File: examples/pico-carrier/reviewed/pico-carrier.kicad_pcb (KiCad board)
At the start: 2 copper layers, 82 x 68 mm, 9 parts, among them J1 5V IN, J3 GP0-GP15, J4 GP16-GP28, PWR, U1 Pico

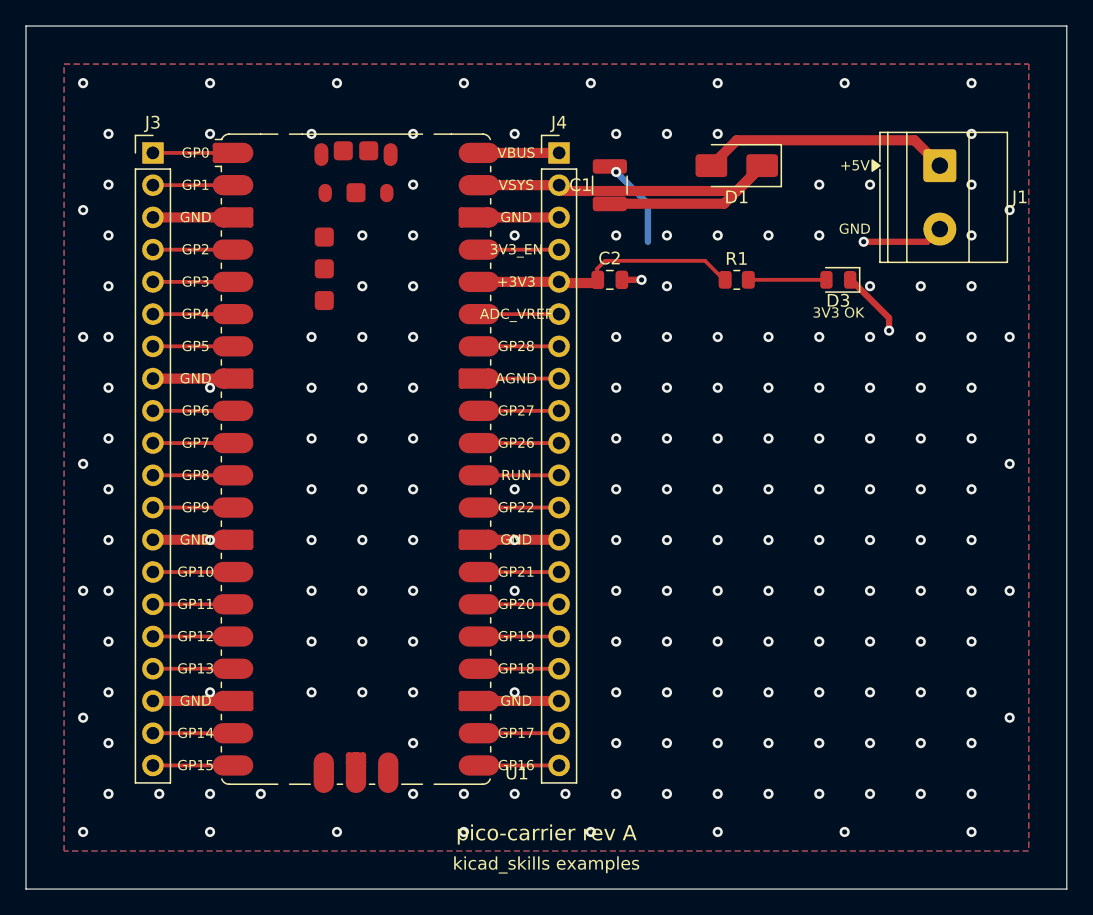
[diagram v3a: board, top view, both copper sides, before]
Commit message: Regenerate the four boards whose corners were off the grid
Ninety-one bends at angles nobody chose, now none. All four still pass
their gates.

Co-Authored-By: Claude Fable 5 <noreply@anthropic.com>
Claude-Session: https://claude.ai/code/session_01DUj7Ltu92tWg159mCSacwY
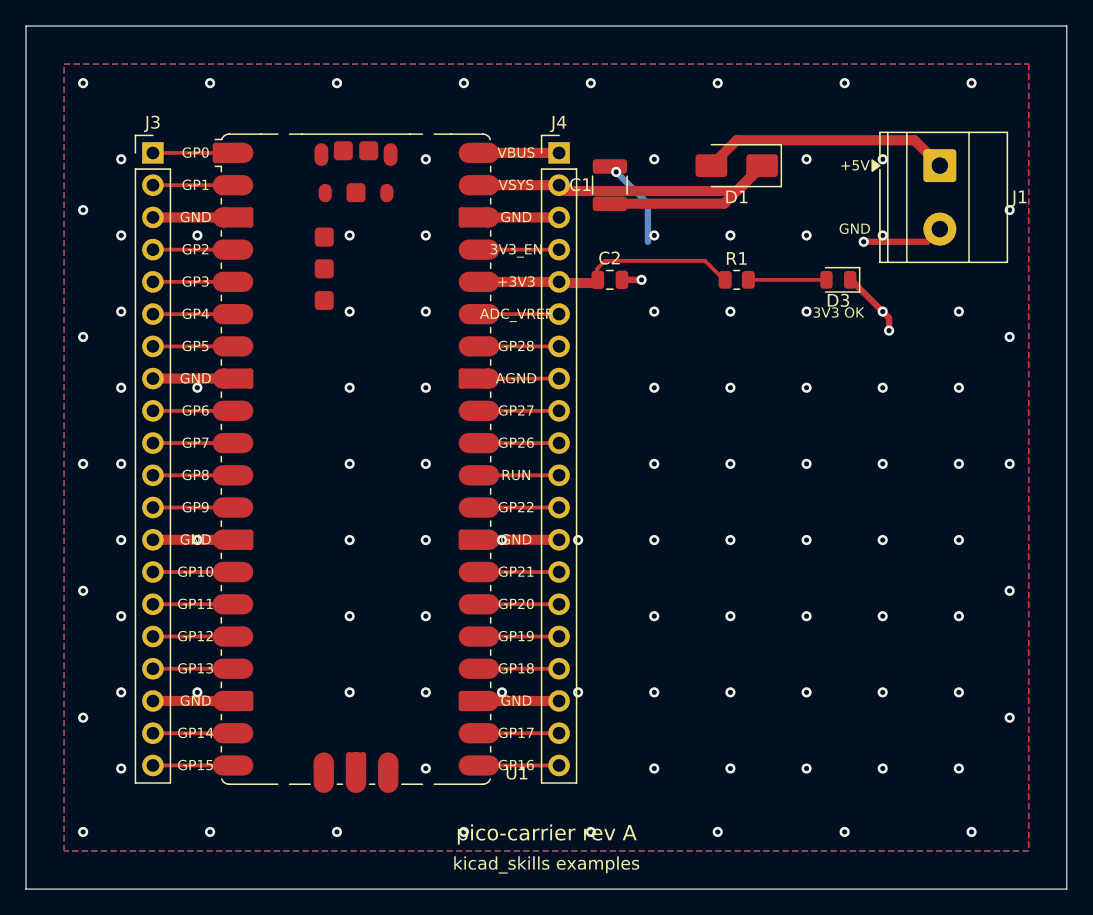
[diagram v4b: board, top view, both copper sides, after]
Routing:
- net GND: track 64.6 -> 64.7 mm, vias 190 -> 105

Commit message: Regenerate the four the text and width work changed
Designators and values off the rails they were printed on, power-named
nets at the width their rule asks for, and the buck's feedback ending
on the capacitor pad it senses at.

Co-Authored-By: Claude Fable 5 <noreply@anthropic.com>
Claude-Session: https://claude.ai/code/session_01DUj7Ltu92tWg159mCSacwY
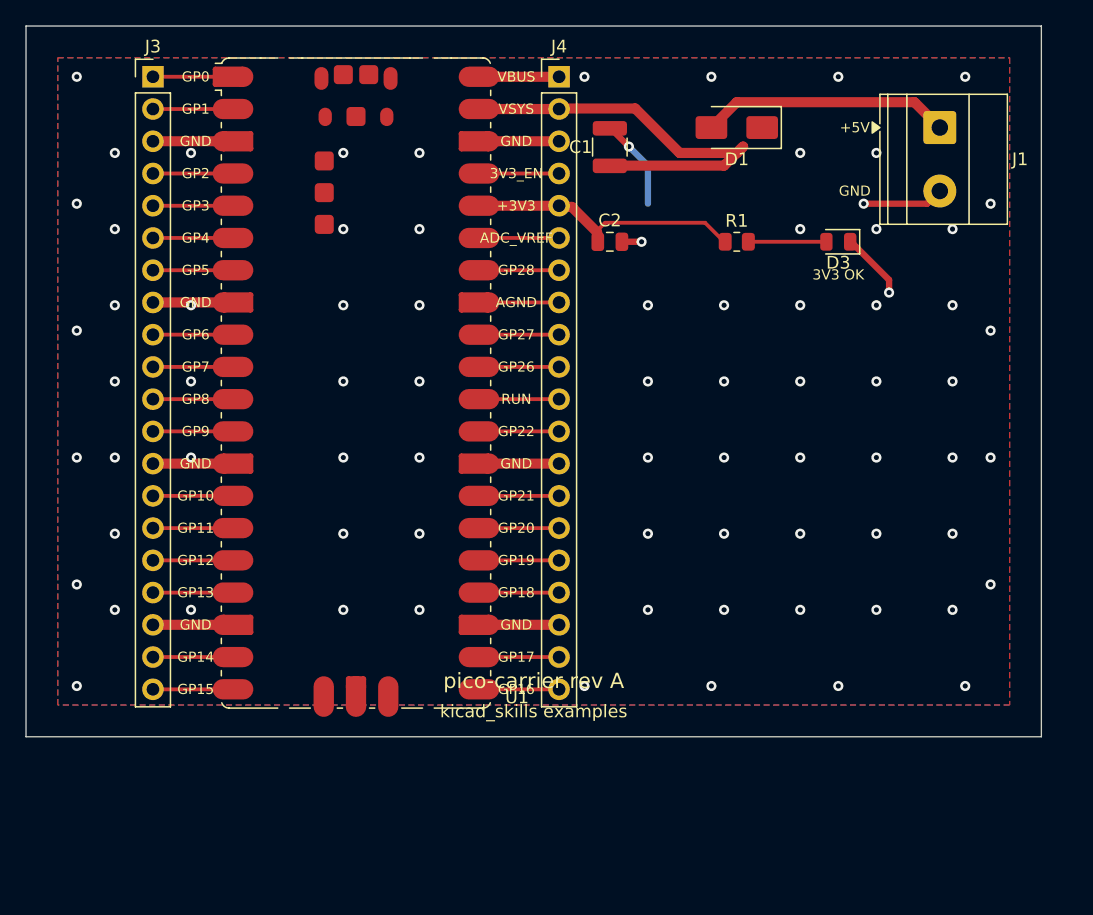
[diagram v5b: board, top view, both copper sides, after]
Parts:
- moved J3 6.00 mm to (110.0, 64.0)
- moved J4 6.00 mm to (142.0, 64.0)
- moved U1 6.00 mm to (126.0, 88.1)
- moved C1 3.00 mm to (146.0, 69.5)
- moved C2 3.00 mm to (146.0, 77.0)
- moved D1 3.00 mm to (156.0, 68.0)
- moved D3 3.00 mm to (164.0, 77.0)
- moved J1 3.00 mm to (172.0, 68.0)
- moved R1 3.00 mm to (156.0, 77.0)
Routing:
- net /VSYS: track 36.6 -> 33.6 mm
- net +3V3: track 21.4 -> 22.8 mm
- net GND: vias 105 -> 78
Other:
- board size 82 x 68 mm -> 80 x 56 mm
